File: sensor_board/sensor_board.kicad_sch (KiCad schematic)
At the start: 45 parts, among them J1 zigbee connector, J2 SWD, J3 Grove-SCD41_Male, J4 Grove-SCD41_Male, J5 Lithium_battery_conn, Q1 SI2300DS, Q2 SI2301DS, U1 MCP6002-xMC, U2 MIC5365-3.3YC5, U3 STM32L051C8Tx

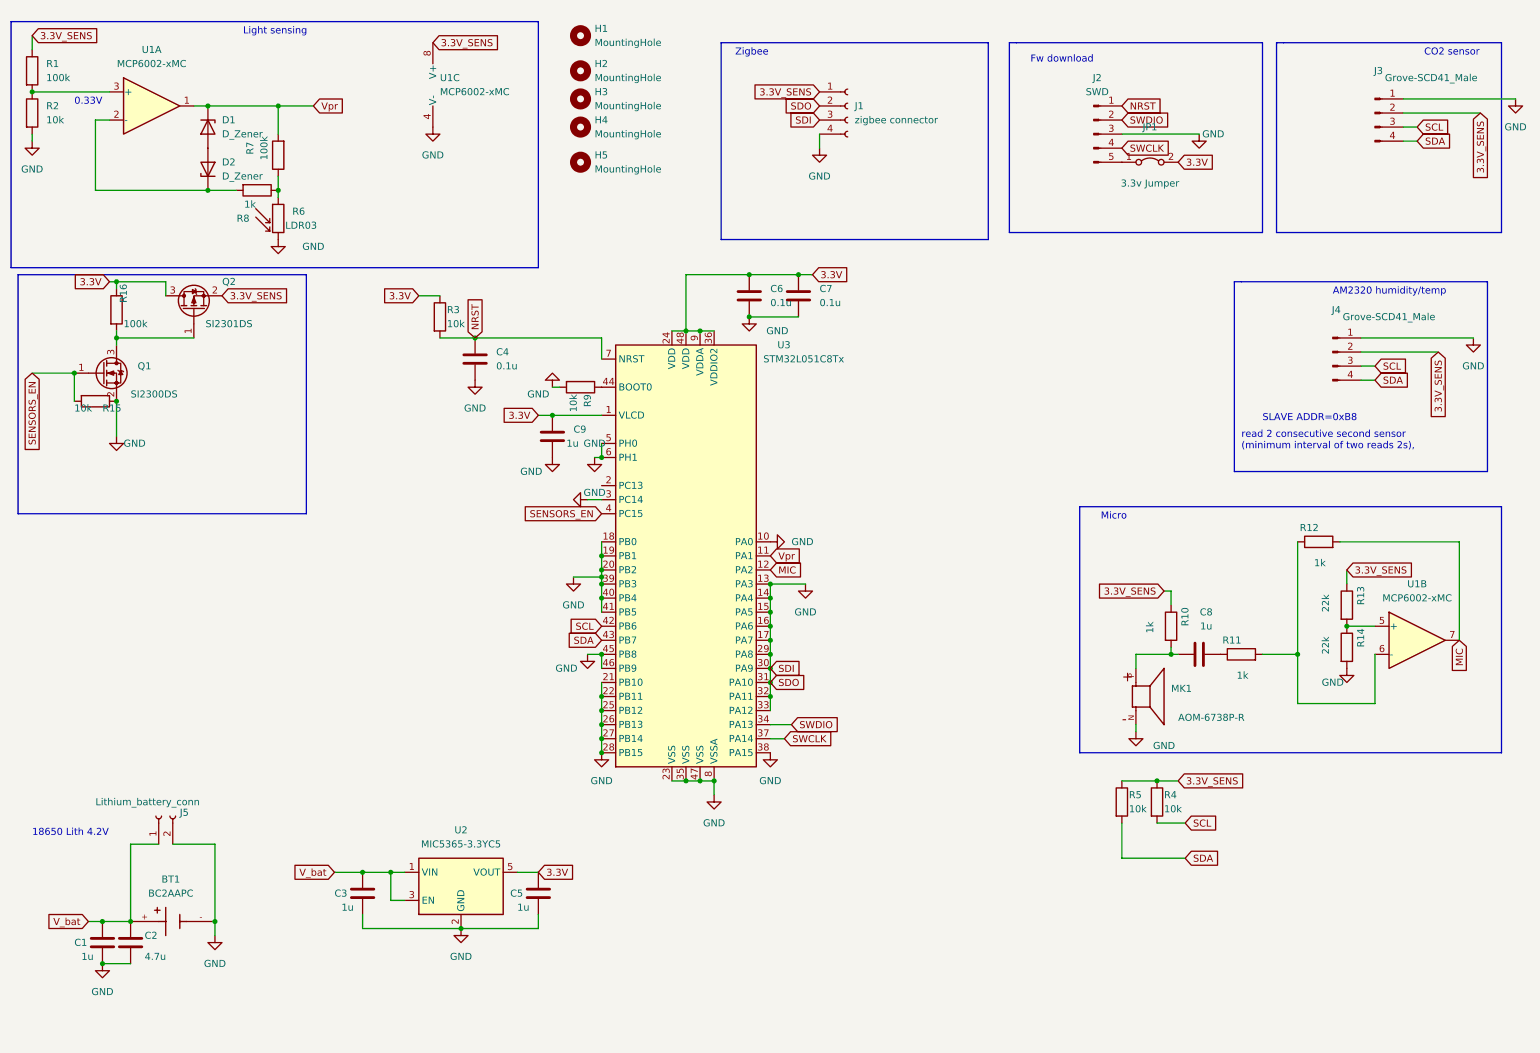
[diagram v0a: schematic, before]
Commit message: replace 2 cells AA with single cell 18650 battery holder
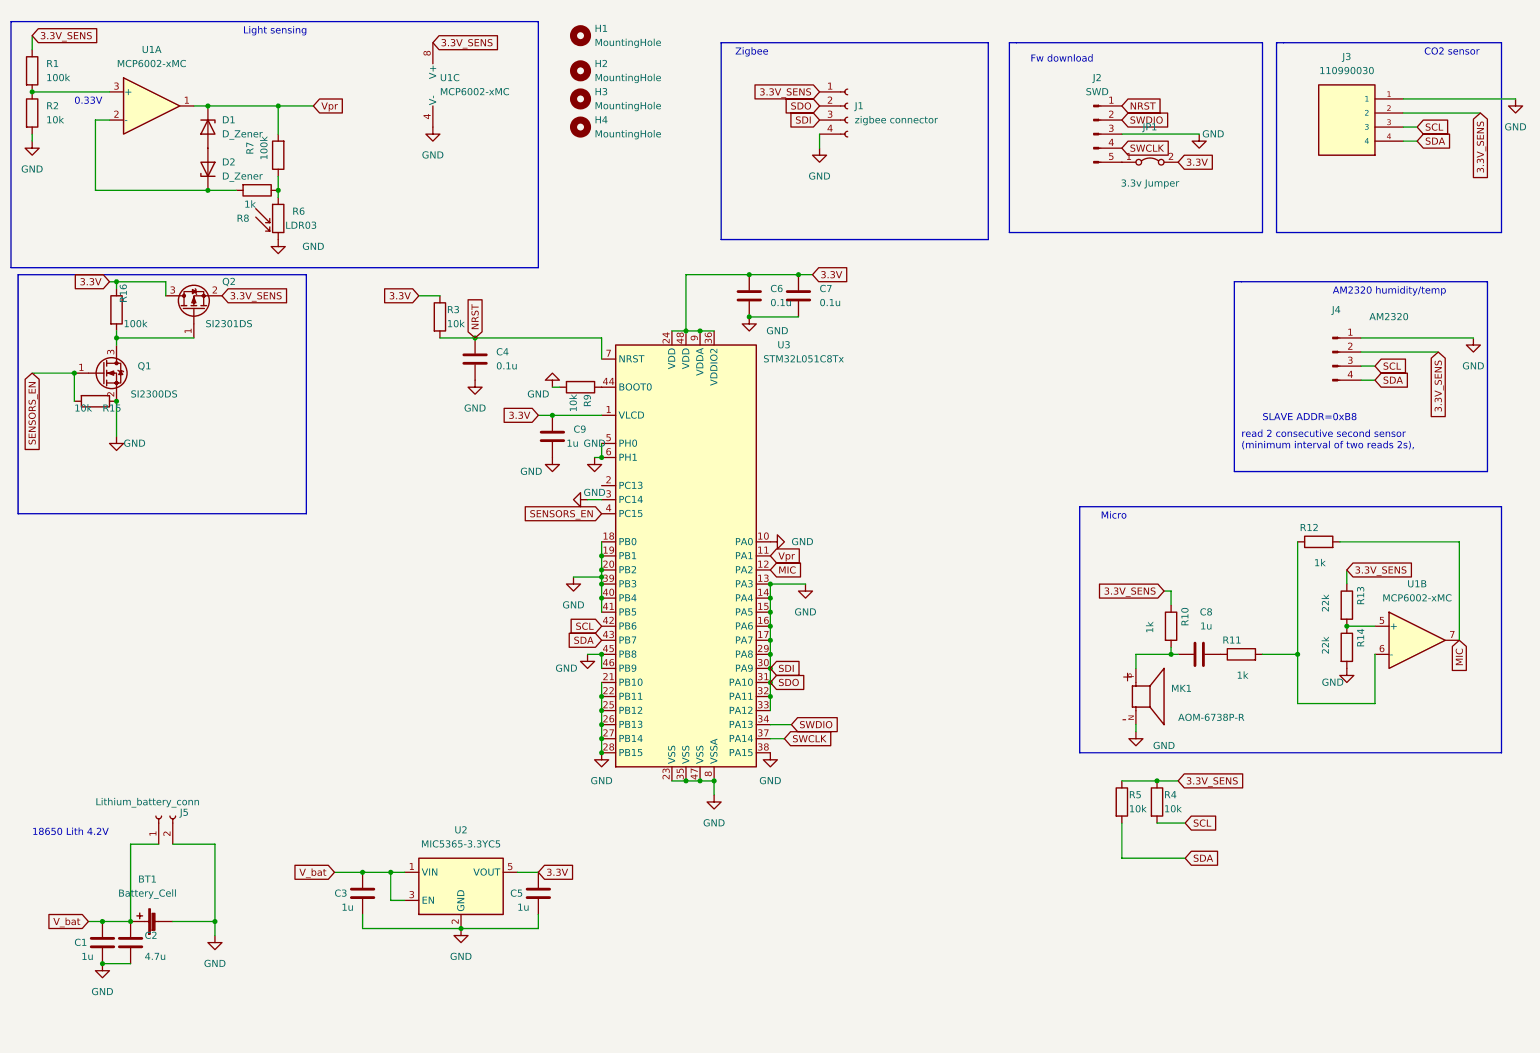
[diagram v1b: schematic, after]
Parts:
- removed BT1: BC2AAPC, BC2AAPC:BAT_BC2AAPC, symbol BC2AAPC:BC2AAPC
- removed H5: MountingHole, MountingHole:MountingHole_2.2mm_M2_Pad, symbol Mechanical:MountingHole
- removed J3: Grove-SCD41_Male, Connector:NS-Tech_Grove_1x04_P2mm_Vertical, symbol Connector:Conn_01x04_Male
- added BT1: Battery_Cell, Battery:BatteryHolder_MPD_BH-18650-PC2, symbol Device:Battery_Cell
- added J3: 110990030, SEEED_110990030, symbol 1x04 grove:110990030
- J4: value Grove-SCD41_Male -> AM2320
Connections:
- net 3.3V_SENS: now also J3.2
- net GND: now also BT1.2 (-), J3.1
- net SCL: now also J3.3
- net SDA: now also J3.4
- net V_bat: now also BT1.1 (+)

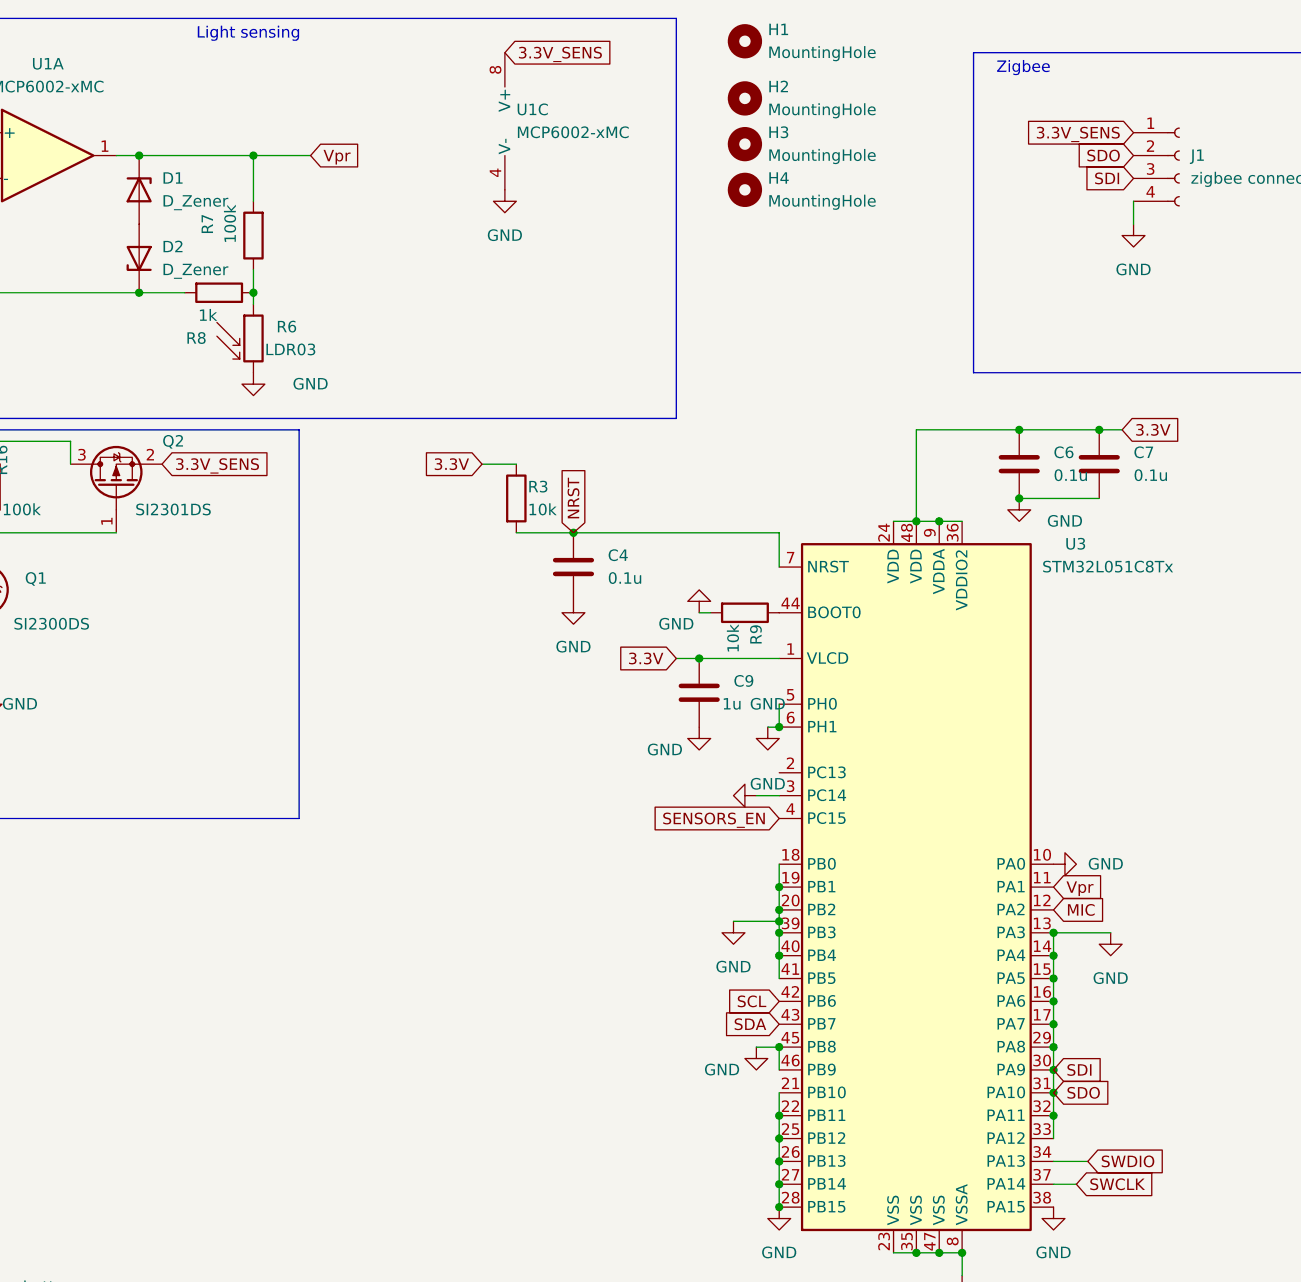
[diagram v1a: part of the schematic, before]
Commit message: modified:   sensor_board/sensor_board.kicad_pcb 	modified:   sensor_board/sensor_board.kicad_sch Fix SDI pins wiring error
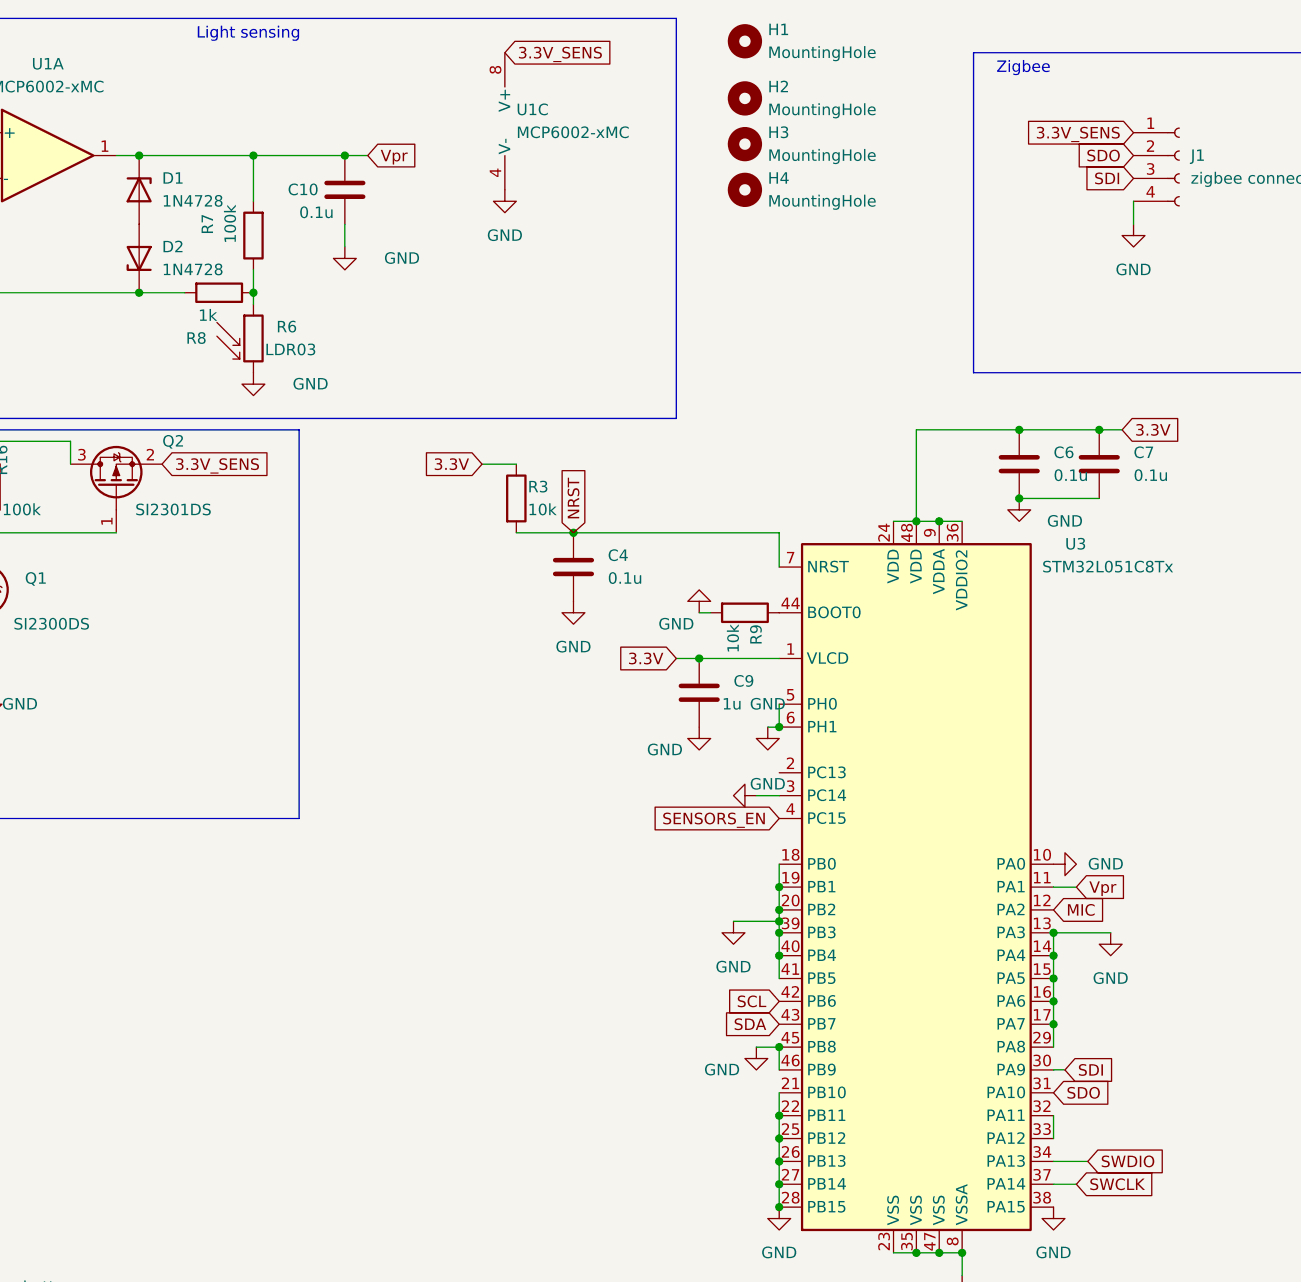
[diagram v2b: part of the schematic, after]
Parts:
- added C10: 0.1u, Capacitor_SMD:C_1206_3216Metric_Pad1.33x1.80mm_HandSolder, symbol Device:C
- D1, D2: value D_Zener -> 1N4728
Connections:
- net GND: now also C10.2; no longer J1.2 (Pin_2), J1.3 (Pin_3), U3.30 (PA9), U3.31 (PA10), U3.32 (PA11), U3.33 (PA12)
- net Vpr: now also C10.1
- new net: U3.32 (PA11), U3.33 (PA12)
- new net SDI: J1.3 (Pin_3), U3.30 (PA9)
- new net SDO: J1.2 (Pin_2), U3.31 (PA10)
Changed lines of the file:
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@@
 (kicad_sch (version 20211123) (generator eeschema)
   (paper "A4")
-  (junction (at 149.86 134.62) (diameter 0) (color 0 0 0 0)
-  )
   (junction (at 119.38 134.62) (diameter 0) (color 0 0 0 0)
   )
@@
   (junction (at 149.86 119.38) (diameter 0) (color 0 0 0 0)
   )
-  (junction (at 149.86 129.54) (diameter 0) (color 0 0 0 0)
-  )
   (junction (at 16.51 25.4) (diameter 0) (color 0 0 0 0)
   )
@@
   (junction (at 119.38 111.76) (diameter 0) (color 0 0 0 0)
   )
-  (junction (at 149.86 132.08) (diameter 0) (color 0 0 0 0)
-  )
   (junction (at 96.52 69.85) (diameter 0) (color 0 0 0 0)
   )
@@
   (junction (at 146.05 66.04) (diameter 0) (color 0 0 0 0)
   )
-  (junction (at 149.86 127) (diameter 0) (color 0 0 0 0)
-  )
   (junction (at 146.05 58.42) (diameter 0) (color 0 0 0 0)
   )
@@
   (junction (at 254 121.92) (diameter 0) (color 0 0 0 0)
   )
+  (junction (at 71.12 27.94) (diameter 0) (color 0 0 0 0)
+  )
   (junction (at 119.38 113.03) (diameter 0) (color 0 0 0 0)
   )
@@
     (stroke (width 0) (type default) (color 0 0 0 0))
   )
+  (wire (pts (xy 71.12 27.94) (xy 73.66 27.94))
+    (stroke (width 0) (type default) (color 0 0 0 0))
+  )
   (wire (pts (xy 114.3 113.03) (xy 119.38 113.03))
     (stroke (width 0) (type default) (color 0 0 0 0))
@@
     (stroke (width 0) (type default) (color 0 0 0 0))
   )
-  (wire (pts (xy 60.96 27.94) (xy 67.31 27.94))
+  (wire (pts (xy 60.96 27.94) (xy 71.12 27.94))
     (stroke (width 0) (type default) (color 0 0 0 0))
   )
@@
     (stroke (width 0) (type default) (color 0 0 0 0))
   )
+  (wire (pts (xy 71.12 38.1) (xy 71.12 35.56))
+    (stroke (width 0) (type default) (color 0 0 0 0))
+  )
   (wire (pts (xy 119.38 114.3) (xy 119.38 116.84))
     (stroke (width 0) (type default) (color 0 0 0 0))
@@
     (stroke (width 0) (type default) (color 0 0 0 0))
   )
-  (wire (pts (xy 149.86 132.08) (xy 149.86 134.62))
-    (stroke (width 0) (type default) (color 0 0 0 0))
-  )
   (wire (pts (xy 40.64 62.23) (xy 40.64 59.69))
     (stroke (width 0) (type default) (color 0 0 0 0))
@@
     (stroke (width 0) (type default) (color 0 0 0 0))
   )
-  (wire (pts (xy 149.86 129.54) (xy 149.86 132.08))
-    (stroke (width 0) (type default) (color 0 0 0 0))
-  )
   (wire (pts (xy 119.38 134.62) (xy 119.38 137.16))
     (stroke (width 0) (type default) (color 0 0 0 0))
@@
     (stroke (width 0) (type default) (color 0 0 0 0))
   )
+  (wire (pts (xy 151.13 129.54) (xy 149.86 129.54))
+    (stroke (width 0) (type default) (color 0 0 0 0))
+  )
   (wire (pts (xy 30.48 30.48) (xy 27.94 30.48))
     (stroke (width 0) (type default) (color 0 0 0 0))
@@
     (stroke (width 0) (type default) (color 0 0 0 0))
   )
-  (wire (pts (xy 149.86 127) (xy 149.86 129.54))
-    (stroke (width 0) (type default) (color 0 0 0 0))
-  )
   (wire (pts (xy 119.38 73.66) (xy 119.38 69.85))
     (stroke (width 0) (type default) (color 0 0 0 0))
@@
   )
   (wire (pts (xy 149.86 121.92) (xy 149.86 124.46))
+    (stroke (width 0) (type default) (color 0 0 0 0))
+  )
+  (wire (pts (xy 152.4 109.22) (xy 149.86 109.22))
     (stroke (width 0) (type default) (color 0 0 0 0))
   )
@@
     (effects (font (size 1.27 1.27)) (justify left bottom))
   )
-  (global_label "Vpr" (shape input) (at 149.86 109.22 0) (fields_autoplaced)
-    (effects (font (size 1.27 1.27)) (justify left))
-    (property "Intersheet References" "${INTERSHEET_REFS}" (id 0) (at 155.2969 109.1406 0)
+  (global_label "Vpr" (shape input) (at 152.4 109.22 0) (fields_autoplaced)
+    (effects (font (size 1.27 1.27)) (justify left))
+    (property "Intersheet References" "${INTERSHEET_REFS}" (id 0) (at 157.8369 109.1406 0)
       (effects (font (size 1.27 1.27)) (justify left) hide)
     )
@@
     )
   )
-  (global_label "SDI" (shape input) (at 149.86 129.54 0) (fields_autoplaced)
-    (effects (font (size 1.27 1.27)) (justify left))
-    (property "Intersheet References" "${INTERSHEET_REFS}" (id 0) (at 155.3574 129.6194 0)
+  (global_label "SDI" (shape input) (at 151.13 129.54 0) (fields_autoplaced)
+    (effects (font (size 1.27 1.27)) (justify left))
+    (property "Intersheet References" "${INTERSHEET_REFS}" (id 0) (at 156.6274 129.6194 0)
       (effects (font (size 1.27 1.27)) (justify left) hide)
     )
@@
     )
   )
-  (global_label "Vpr" (shape input) (at 67.31 27.94 0) (fields_autoplaced)
-    (effects (font (size 1.27 1.27)) (justify left))
-    (property "Intersheet References" "${INTERSHEET_REFS}" (id 0) (at 72.7469 27.8606 0)
+  (global_label "Vpr" (shape input) (at 73.66 27.94 0) (fields_autoplaced)
+    (effects (font (size 1.27 1.27)) (justify left))
+    (property "Intersheet References" "${INTERSHEET_REFS}" (id 0) (at 79.0969 27.8606 0)
       (effects (font (size 1.27 1.27)) (justify left) hide)
     )
@@
     (pin "2")
   )
+  (symbol (lib_name "GND_1") (lib_id "power:GND") (at 71.12 38.1 0) (unit 1)
+    (in_bom yes) (on_board yes)
+    (property "Reference" "#PWR0101" (id 0) (at 71.12 44.45 0)
+      (effects (font (size 1.27 1.27)) hide)
+    )
+    (property "Value" "GND" (id 1) (at 77.47 39.37 0))
+    (property "Footprint" "" (id 2) (at 71.12 38.1 0)
+      (effects (font (size 1.27 1.27)) hide)
+    )
+    (property "Datasheet" "" (id 3) (at 71.12 38.1 0)
+      (effects (font (size 1.27 1.27)) hide)
+    )
+    (pin "1")
+  )
   (symbol (lib_id "power:GND") (at 149.86 106.68 90) (unit 1)
     (in_bom yes) (on_board yes) (fields_autoplaced)
@@
     (pin "2")
   )
+  (symbol (lib_id "Device:C") (at 71.12 31.75 0) (unit 1)
+    (in_bom yes) (on_board yes)
+    (property "Reference" "C10" (id 0) (at 64.77 31.75 0)
+      (effects (font (size 1.27 1.27)) (justify left))
+    )
+    (property "Value" "0.1u" (id 1) (at 66.04 34.29 0)
+      (effects (font (size 1.27 1.27)) (justify left))
+    )
+    (property "Footprint" "Capacitor_SMD:C_1206_3216Metric_Pad1.33x1.80mm_HandSolder" (id 2) (at 72.0852 35.56 0)
+      (effects (font (size 1.27 1.27)) hide)
+    )
+    (property "Datasheet" "~" (id 3) (at 71.12 31.75 0)
+      (effects (font (size 1.27 1.27)) hide)
+    )
+    (pin "1")
+    (pin "2")
+  )
   (symbol (lib_id "Device:C") (at 96.52 73.66 0) (unit 1)
     (in_bom yes) (on_board yes) (fields_autoplaced)
@@
       (effects (font (size 1.27 1.27)) (justify left))
     )
-    (property "Value" "D_Zener" (id 1) (at 50.8 33.0199 90)
+    (property "Value" "1N4728" (id 1) (at 50.8 33.0199 90)
       (effects (font (size 1.27 1.27)) (justify left))
     )
@@
       (effects (font (size 1.27 1.27)) (justify right))
     )
-    (property "Value" "D_Zener" (id 1) (at 50.8 40.6399 90)
+    (property "Value" "1N4728" (id 1) (at 50.8 40.6399 90)
       (effects (font (size 1.27 1.27)) (justify right))
     )
@@
       (reference "#PWR026") (unit 1) (value "GND") (footprint "")
     )
+    (path "/50498d08-b5b7-4110-8645-ab500d9bb0b8"
+      (reference "#PWR0101") (unit 1) (value "GND") (footprint "")
+    )
     (path "/3d46b2d1-d4c6-445c-8019-d8d536518f09"
       (reference "BT1") (unit 1) (value "Battery_Cell") (footprint "Battery:BatteryHolder_MPD_BH-18650-PC2")
@@
       (reference "C9") (unit 1) (value "1u") (footprint "Capacitor_SMD:C_1206_3216Metric_Pad1.33x1.80mm_HandSolder")
     )
+    (path "/61cae79c-c842-4095-b504-cb660de3a03c"
+      (reference "C10") (unit 1) (value "0.1u") (footprint "Capacitor_SMD:C_1206_3216Metric_Pad1.33x1.80mm_HandSolder")
+    )
     (path "/9b920d04-02f2-4962-996b-687e6ddffa2c"
-      (reference "D1") (unit 1) (value "D_Zener") (footprint "Diode_SMD:D_SOD-110")
+      (reference "D1") (unit 1) (value "1N4728") (footprint "Diode_SMD:D_SOD-110")
     )
     (path "/ddcdc6af-f280-491e-a36f-9e54f23a0229"
-      (reference "D2") (unit 1) (value "D_Zener") (footprint "Diode_SMD:D_SOD-110")
+      (reference "D2") (unit 1) (value "1N4728") (footprint "Diode_SMD:D_SOD-110")
     )
     (path "/71e07aa7-cede-43bf-87af-b97ea41a3c69"
